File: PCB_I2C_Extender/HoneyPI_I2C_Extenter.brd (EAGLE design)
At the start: 67.8 x 40 mm, 14 parts

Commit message: Update...
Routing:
- net N$1: track 0.00 -> 5.39 mm
- net N$2: track 0.00 -> 5.39 mm
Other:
- board text added: "Use shielded but NOT for SDA SCL twisted pairs cable. CAT5 is fine."
- board text removed: "Use shielded twisted pair cable at least. CAT5 is fine."
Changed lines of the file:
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@@
 <vertex x="54.61" y="7.62"/>
 </spline>
-<text x="52.07" y="8.89" size="0.8128" layer="1">Use shielded twisted
-pair cable at least.
+<text x="50.8" y="10.16" size="0.8128" layer="1">Use shielded but
+NOT for SDA SCL twisted pairs
+cable.
 CAT5 is fine.</text>
 <text x="5.969" y="22.606" size="0.8128" layer="1">GND
@@
 <wire x1="15.1554" y1="30.5629" x2="15.24" y2="30.48" width="0.1524" layer="16"/>
 </signal>
+<signal name="N$1">
+<wire x1="57.15" y1="8.89" x2="60.96" y2="5.08" width="0.1524" layer="1"/>
+</signal>
+<signal name="N$2">
+<wire x1="59.69" y1="8.89" x2="55.88" y2="5.08" width="0.1524" layer="1"/>
+</signal>
 </signals>

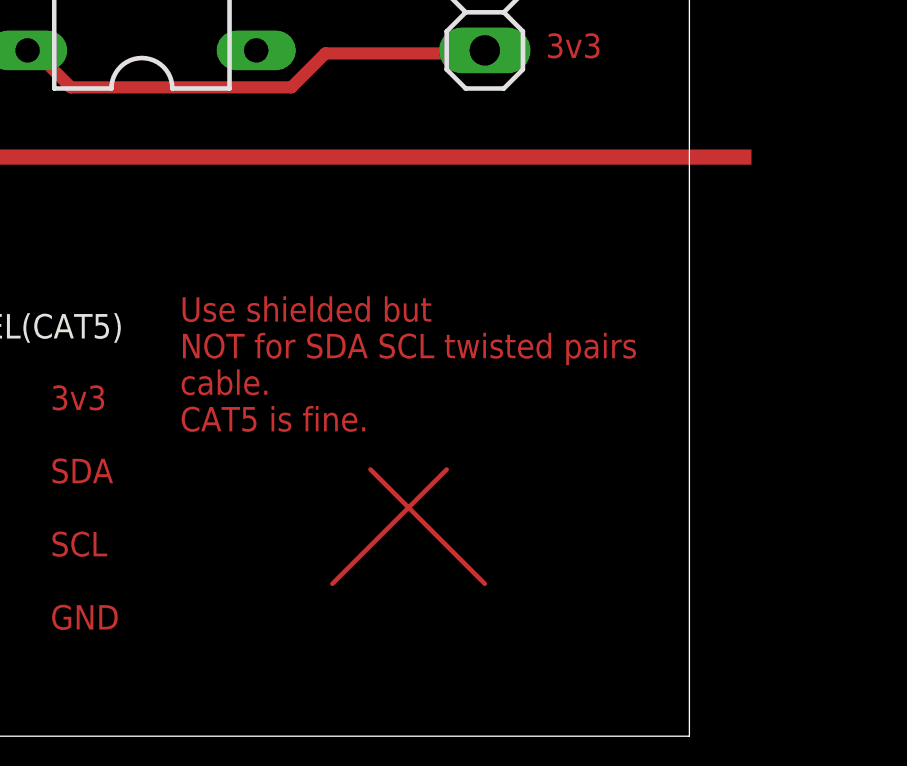
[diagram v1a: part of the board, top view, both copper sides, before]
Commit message: Twisted pairs cable info
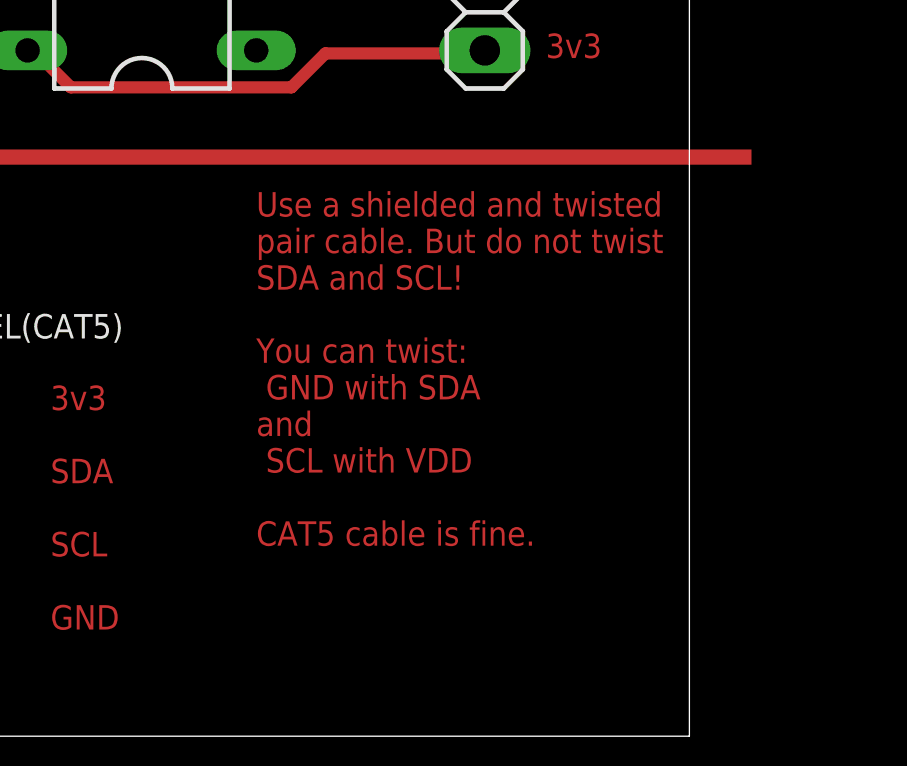
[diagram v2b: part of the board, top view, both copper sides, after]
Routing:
- net N$1: track 5.39 -> 0.00 mm
- net N$2: track 5.39 -> 0.00 mm
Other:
- board text added: "Use a shielded and twisted pair cable. But do not twist SDA and SCL! You can twist: GND with SDA and SCL with VDD CAT5 cable is fine."
- board text removed: "Use shielded but NOT for SDA SCL twisted pairs cable. CAT5 is fine."
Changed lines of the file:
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@@
 4K7   3K1</text>
 <spline width="0.1524" layer="20" locked="no">
-<vertex x="53.34" y="7.62"/>
-<vertex x="56.30333125" y="3.386665625"/>
-<vertex x="57.361665625" y="10.58333125"/>
-<vertex x="62.23" y="6.35"/>
+<vertex x="55.88" y="5.08"/>
+<vertex x="58.84333125" y="0.846665625"/>
+<vertex x="59.901665625" y="8.04333125"/>
+<vertex x="64.77" y="3.81"/>
 </spline>
 <spline width="0.1524" layer="20" locked="no">
-<vertex x="63.5" y="6.35"/>
-<vertex x="60.53666875" y="10.583334375"/>
-<vertex x="59.478334375" y="3.38666875"/>
-<vertex x="54.61" y="7.62"/>
+<vertex x="66.04" y="3.81"/>
+<vertex x="63.07666875" y="8.043334375"/>
+<vertex x="62.018334375" y="0.84666875"/>
+<vertex x="57.15" y="5.08"/>
 </spline>
-<text x="50.8" y="10.16" size="0.8128" layer="1">Use shielded but
-NOT for SDA SCL twisted pairs
-cable.
-CAT5 is fine.</text>
+<text x="53.34" y="6.35" size="0.8128" layer="1">Use a shielded and twisted
+pair cable. But do not twist
+SDA and SCL!
+You can twist:
+ GND with SDA
+and
+ SCL with VDD
+CAT5 cable is fine.</text>
 <text x="5.969" y="22.606" size="0.8128" layer="1">GND
 SCL
@@
 NC</text>
 <rectangle x1="-1.27" y1="19.05" x2="69.85" y2="19.558" layer="1"/>
+<spline width="0.1524" layer="20" locked="no">
+<vertex x="55.88" y="2.54"/>
+<vertex x="58.84333125" y="-1.693334375"/>
+<vertex x="59.901665625" y="5.50333125"/>
+<vertex x="64.77" y="1.27"/>
+</spline>
+<spline width="0.1524" layer="20" locked="no">
+<vertex x="66.04" y="1.27"/>
+<vertex x="63.07666875" y="5.503334375"/>
+<vertex x="62.018334375" y="-1.69333125"/>
+<vertex x="57.15" y="2.54"/>
+</spline>
 </plain>
 <attributes>
@@
 <wire x1="15.1554" y1="30.5629" x2="15.24" y2="30.48" width="0.1524" layer="16"/>
 </signal>
-<signal name="N$1">
-<wire x1="57.15" y1="8.89" x2="60.96" y2="5.08" width="0.1524" layer="1"/>
-</signal>
-<signal name="N$2">
-<wire x1="59.69" y1="8.89" x2="55.88" y2="5.08" width="0.1524" layer="1"/>
-</signal>
 </signals>
